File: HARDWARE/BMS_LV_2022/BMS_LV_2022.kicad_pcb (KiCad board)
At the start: 4 copper layers, 90 x 45 mm, 157 parts, among them J1 Conn_01x06_Male, J11 Conn_01x07_Female, J12 Conn_01x08_Female, J2 Conn_01x12_Male, J3 USB_B_Mini, J4 Battery+, J5 Battery-, Q1 BC846, Q10 BSS138, Q11 SiSS05DN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

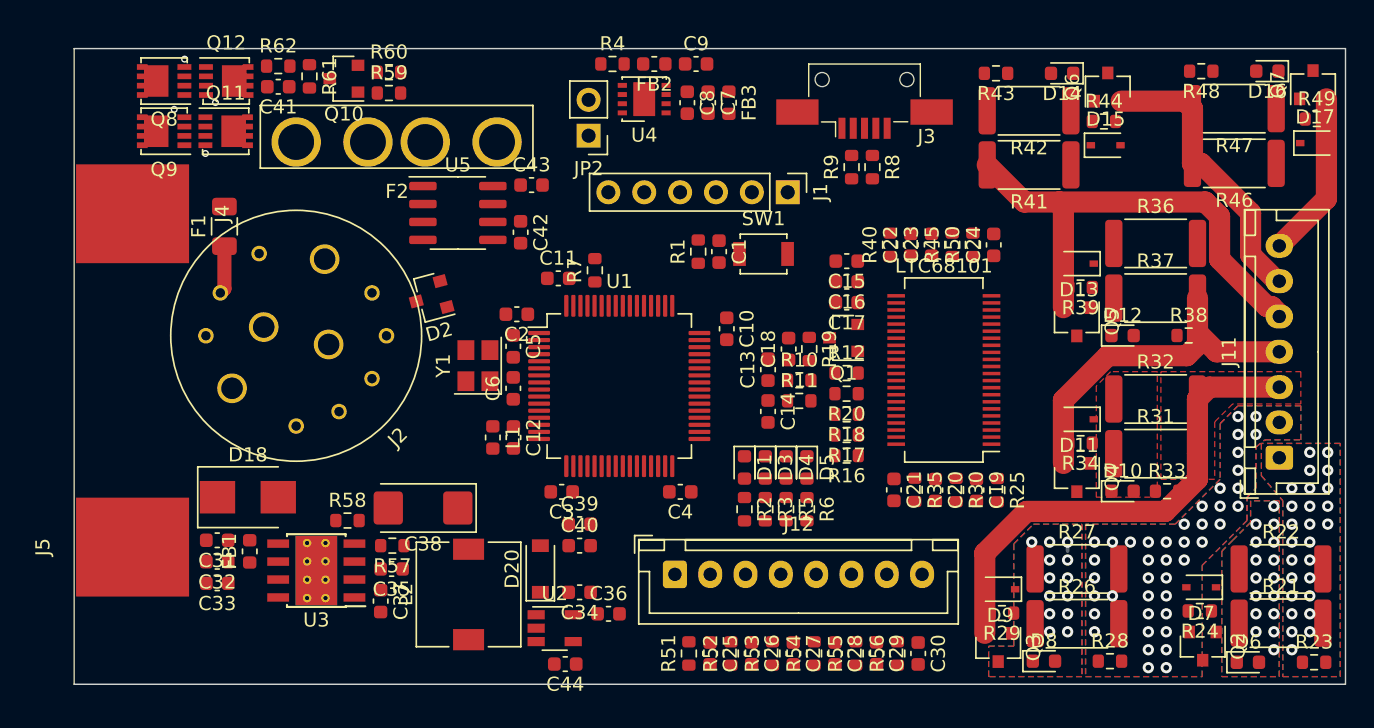
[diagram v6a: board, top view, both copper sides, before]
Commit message: PCB Routing Update
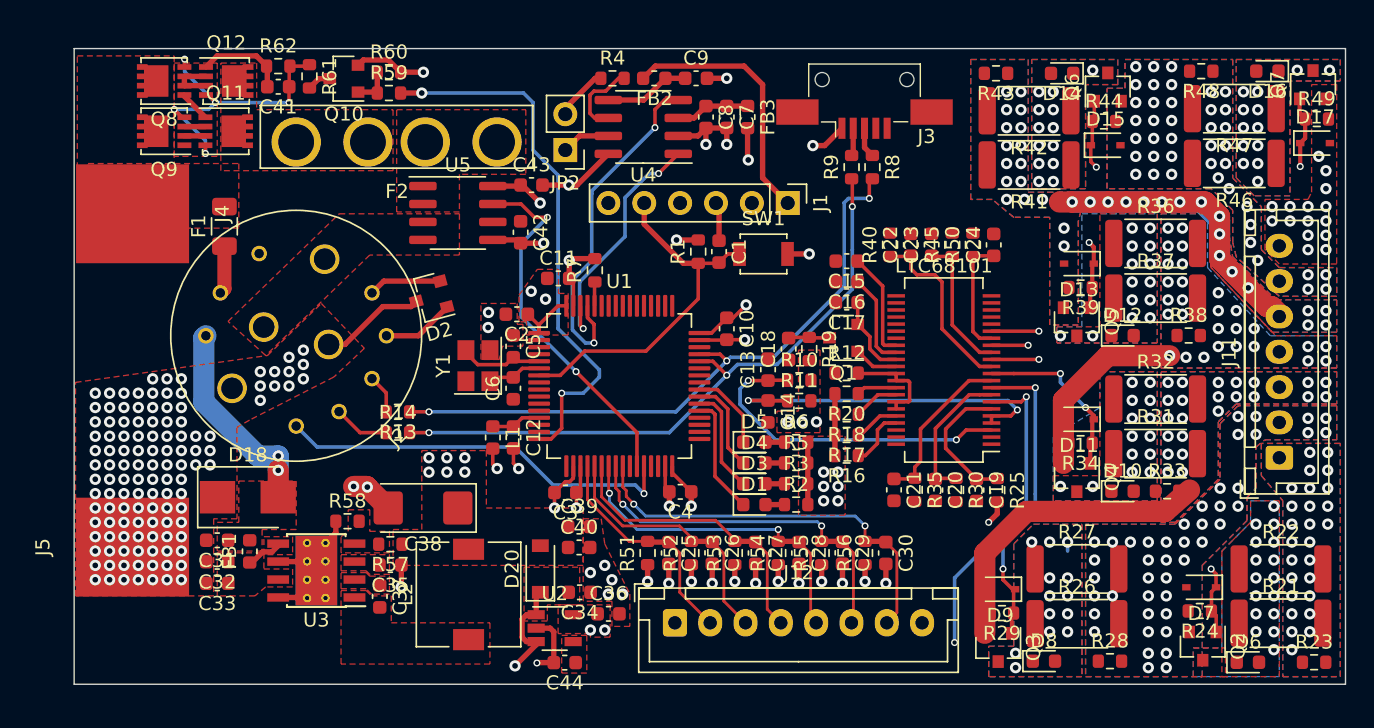
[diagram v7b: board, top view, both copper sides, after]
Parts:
- added R13: 30, Resistor_SMD:R_0603_1608Metric, F.Cu at (132.9, 105.7)
- added R14: 30, Resistor_SMD:R_0603_1608Metric, F.Cu at (132.9, 107.2)
- U4: footprint Package_DFN_QFN:DFN-8-1EP_3x3mm_P0.65mm_EP1.55x2.4mm -> Package_SO:SOIC-8_3.9x4.9mm_P1.27mm
- moved C25 7.69 mm to (152.1, 115.7)
- moved R51 7.69 mm to (150.6, 115.7)
- moved R52 7.64 mm to (153.7, 115.7)
- moved C26 7.64 mm to (155.2, 115.7)
- moved R53 7.60 mm to (156.8, 115.7)
- moved C27 7.60 mm to (158.2, 115.7)
- moved R54 7.55 mm to (159.8, 115.7)
- moved C28 7.55 mm to (161.3, 115.7)
- moved R55 7.51 mm to (162.9, 115.7)
- moved C29 7.51 mm to (164.4, 115.7)
- moved C30 7.47 mm to (167.5, 115.7)
- moved R56 7.47 mm to (166.0, 115.7)
- moved R6 4.81 mm to (161.1, 107.9), turned to 0 degrees
- moved D5 4.13 mm to (158.2, 107.9), turned to 0 degrees
- moved R2 3.67 mm to (161.1, 112.3), turned to 0 degrees
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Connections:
- J2 pad 3: /Interlock -> Net-(J2-Pad3)
- J2 pad 4: /USB-DM -> Net-(J2-Pad4)
- J2 pad 5: /USB-DP -> /Interlock
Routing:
- net +5VD: track 0.00 -> 88.0 mm, vias 0 -> 2
- net GND: track 0.00 -> 74.6 mm, vias 0 -> 147
- net +3V3: track 0.00 -> 53.1 mm, vias 0 -> 21
- net /LTC6810/Balance1/Sx: track 0.00 -> 48.7 mm, vias 0 -> 3
- net /USB-DP: track 0.00 -> 45.9 mm, vias 0 -> 3
- net /USB-DM: track 0.00 -> 45.7 mm, vias 0 -> 3
- net +5V: track 0.00 -> 44.9 mm, vias 0 -> 8
- net /Switch_Signal: track 0.00 -> 38.6 mm, vias 0 -> 2
- net /LTC6810/Balance6/Sx: track 0.00 -> 35.6 mm, vias 0 -> 2
- net /Therm_6: track 0.00 -> 28.9 mm, vias 0 -> 2
- net /Interlock: track 0.00 -> 28.5 mm, vias 0 -> 1
- net /Therm_5: track 0.00 -> 26.3 mm, vias 0 -> 2
- net /CurrentSensor_Out: track 0.00 -> 26.0 mm, vias 0 -> 2
- net /NRST: track 0.00 -> 25.7 mm
- net Net-(C14-Pad1): track 0.00 -> 24.7 mm, vias 0 -> 2
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- added copper zone on F.Cu, net +24V
- added copper zone on F.Cu, net +3V3
- added copper zone on In1.Cu, net +3V3
- added copper zone on F.Cu, net +5V
- added copper zone on In1.Cu, net +5V
- added copper zone on F.Cu, net +5VD
- added copper zone on In1.Cu, net +BATT
- added copper zone on F.Cu, net /CS_IP+
- added copper zone on In1.Cu, net /LTC6810/CellBalance2
- added copper zone on B.Cu, net /LTC6810/CellBalance3
- added copper zone on B.Cu, net /LTC6810/CellBalance4
- added copper zone on F.Cu, net /LTC6810/CellBalance4
- added copper zone on B.Cu, net /LTC6810/CellBalance5
- added copper zone on F.Cu, net /LTC6810/CellBalance5
- added copper zone on B.Cu, net /LTC6810/CellBalance6
- added copper zone on F.Cu, net /LTC6810/CellBalance6
- added copper zone on F.Cu, net /V_Out
- added copper zone on F.Cu, net GND
- added copper zone on F.Cu, net GNDPWR
- added copper zone on F.Cu, net Net-(C32-Pad1)
- added copper zone on F.Cu, net Net-(C35-Pad2)
- added copper zone on F.Cu, net Net-(C37-Pad1)
- added copper zone on F.Cu, net Net-(C37-Pad2)
- added copper zone on F.Cu, net Net-(C41-Pad2)
- added copper zone on F.Cu, net Net-(C44-Pad1)
- added copper zone on B.Cu, net Net-(D10-Pad1)
- added copper zone on B.Cu, net Net-(D12-Pad1)
- added copper zone on F.Cu, net Net-(D12-Pad1)
- added copper zone on B.Cu, net Net-(D14-Pad1)
- added copper zone on F.Cu, net Net-(D14-Pad1)
- added copper zone on B.Cu, net Net-(D16-Pad1)
- added copper zone on F.Cu, net Net-(D16-Pad1)
- added copper zone on F.Cu, net Net-(F2-Pad2)
- added copper zone on F.Cu, net Net-(R57-Pad2)
- added copper zone on F.Cu, net VCC

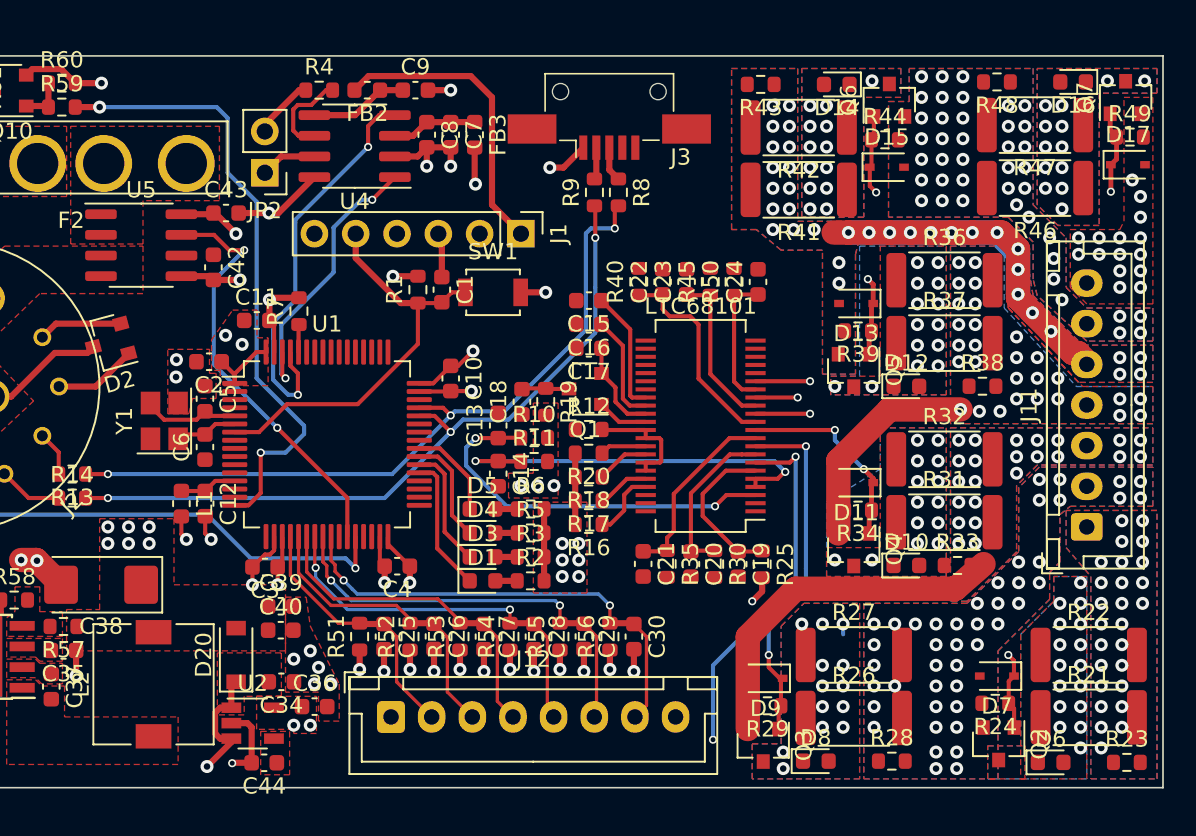
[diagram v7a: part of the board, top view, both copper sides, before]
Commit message: PCB Routing Update 2
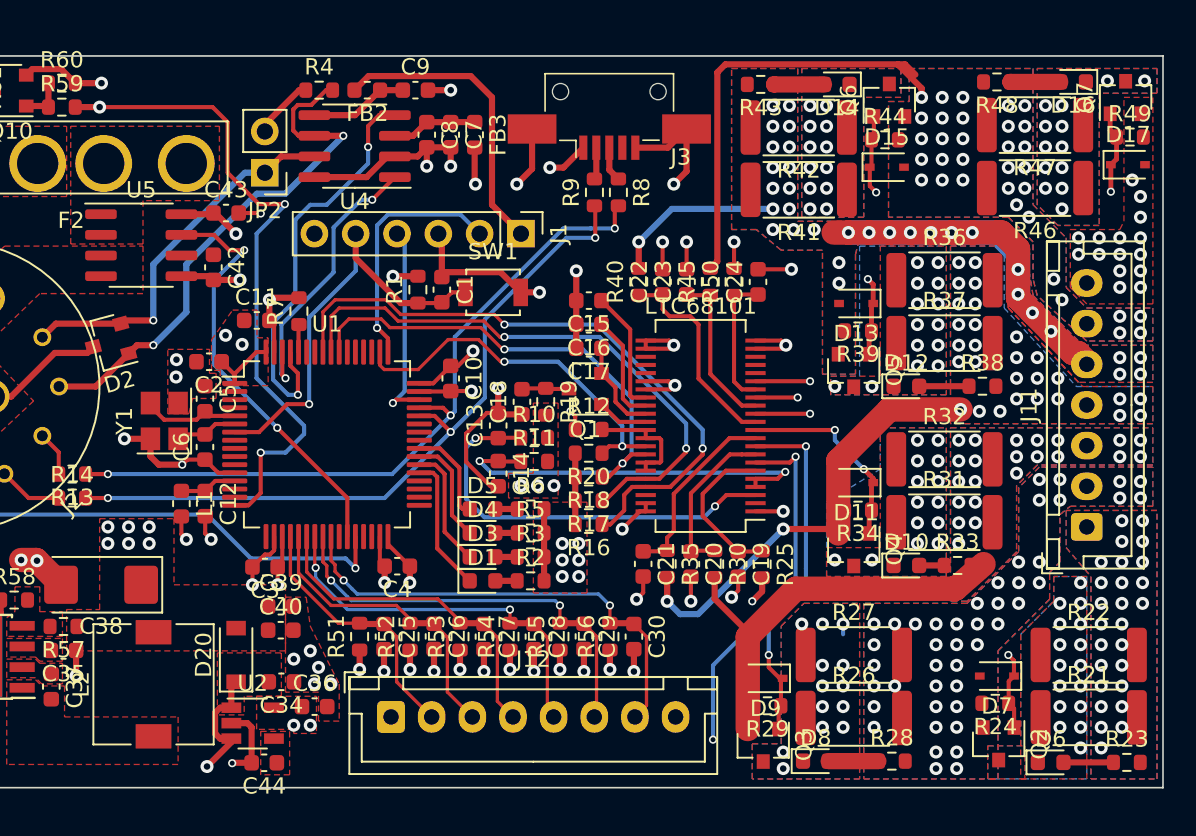
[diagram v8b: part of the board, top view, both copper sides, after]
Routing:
- net GNDPWR: track 0.00 -> 43.5 mm, vias 15 -> 30
- net /MOSI: track 4.20 -> 39.5 mm, vias 0 -> 2
- net /MISO: track 3.24 -> 35.3 mm, vias 0 -> 2
- net /LTC6810/CellBalance6: track 0.17 -> 27.7 mm, vias 41 -> 33
- net GND: track 74.6 -> 100.6 mm, vias 147 -> 151
- net /SCK: track 3.26 -> 29.2 mm, vias 0 -> 2
- net /CANL: track 10.8 -> 33.0 mm, vias 0 -> 2
- net /CS: track 2.86 -> 22.9 mm, vias 0 -> 2
- net /SW-CLK: track 0.00 -> 15.2 mm, vias 0 -> 1
- net /CANH: track 8.63 -> 23.4 mm, vias 0 -> 1
- net /LTC6810/CellBalance4: track 13.3 -> 27.9 mm, vias 28 -> 30
- net /SW-DIO: track 0.00 -> 12.6 mm, vias 0 -> 1
- net /LTC6810/CellBalance5: track 34.3 -> 45.0 mm, vias 34 -> 33
- net /LTC6810/CellBalance3: track 22.0 -> 26.5 mm, vias 23 -> 22
- net Net-(D6-Pad2): track 0.00 -> 3.07 mm
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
